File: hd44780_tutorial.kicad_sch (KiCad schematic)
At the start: 28 parts, among them J1 LCD_2004_PinSocket_1x16_P2.54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, J2 USB4105-GF-A, SW1 REG SELECT, SW2 ENABLE, SW3 DS02C-254-1L-08BE

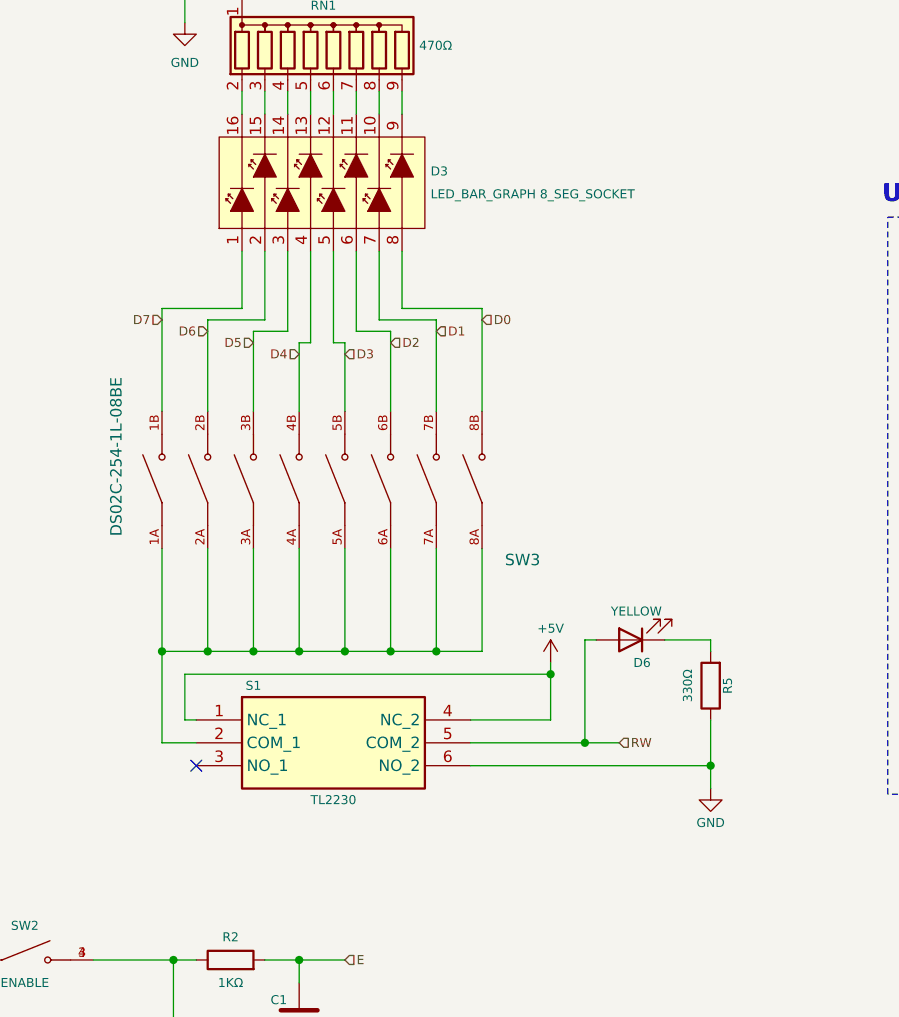
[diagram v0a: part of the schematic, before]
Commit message: Fixed wiring on the TL2230 switch. Made more space between switches and LEDs. New gerbers and JPEG.
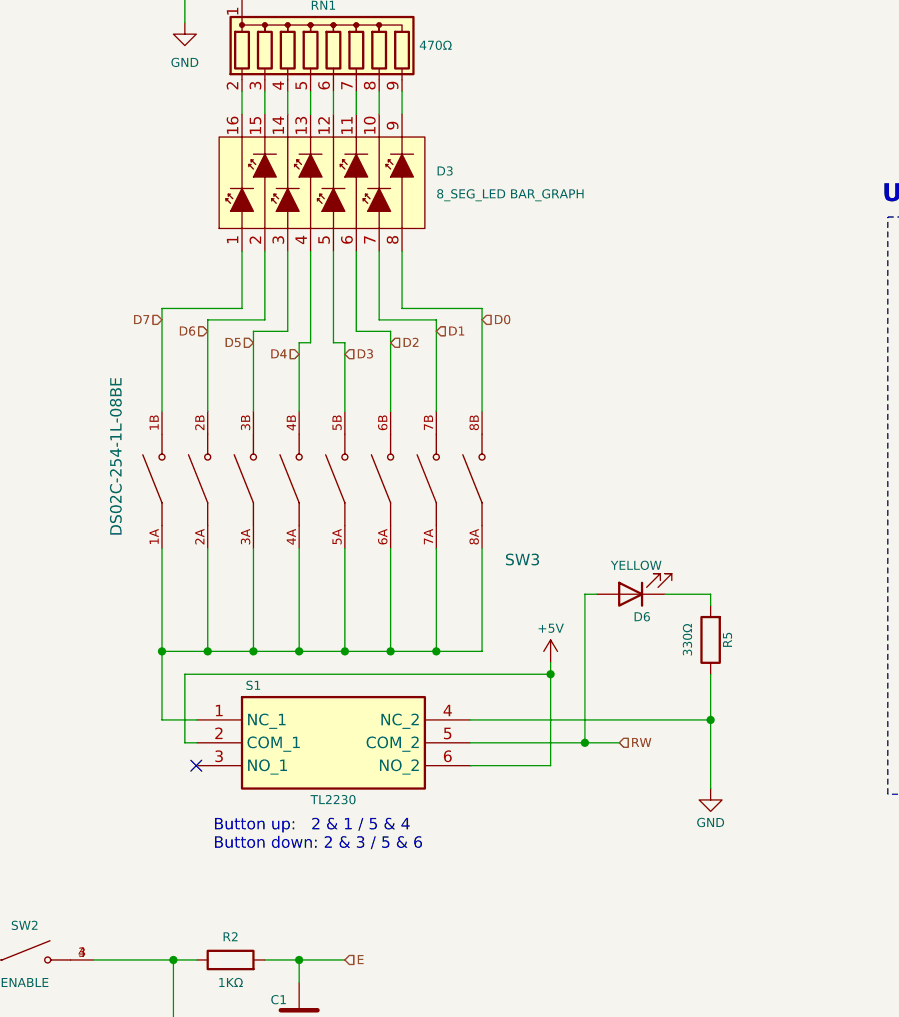
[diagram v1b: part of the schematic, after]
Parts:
- D3: value LED_BAR_GRAPH 8_SEG_SOCKET -> 8_SEG_LED BAR_GRAPH
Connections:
- net +5V: now also S1.2 (COM_1), S1.6 (NO_2); no longer S1.1 (NC_1), S1.4 (NC_2)
- net GND: now also S1.4 (NC_2); no longer S1.6 (NO_2)
- net at SW3.1A, SW3.2A, SW3.3A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: now also S1.1 (NC_1); no longer S1.2 (COM_1)
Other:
- note added: "Button up: 2 & 1 / 5 & 4 Button down: 2 & 3 / 5 & 6"
- moved on the sheet: D6, R5
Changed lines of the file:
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@@
   (title_block
     (title "${project_name}")
-    (date "2024-02-24")
+    (date "2024-03-05")
     (rev "${version}")
   )
@@
   (junction (at 204.47 106.68) (diameter 0) (color 0 0 0 0)
   )
+  (junction (at 58.42 95.25) (diameter 0) (color 0 0 0 0)
+  )
+  (junction (at 133.35 120.65) (diameter 0) (color 0 0 0 0)
+  )
+  (junction (at 58.42 83.82) (diameter 0) (color 0 0 0 0)
+  )
+  (junction (at 102.87 120.65) (diameter 0) (color 0 0 0 0)
+  )
+  (junction (at 17.78 92.71) (diameter 0) (color 0 0 0 0)
+  )
+  (junction (at 163.83 128.27) (diameter 0) (color 0 0 0 0)
+  )
+  (junction (at 118.11 175.26) (diameter 0) (color 0 0 0 0)
+  )
+  (junction (at 128.27 120.65) (diameter 0) (color 0 0 0 0)
+  )
+  (junction (at 204.47 93.98) (diameter 0) (color 0 0 0 0)
+  )
   (junction (at 146.05 123.19) (diameter 0) (color 0 0 0 0)
-  )
-  (junction (at 58.42 95.25) (diameter 0) (color 0 0 0 0)
-  )
-  (junction (at 133.35 120.65) (diameter 0) (color 0 0 0 0)
-  )
-  (junction (at 58.42 83.82) (diameter 0) (color 0 0 0 0)
-  )
-  (junction (at 102.87 120.65) (diameter 0) (color 0 0 0 0)
-  )
-  (junction (at 163.83 133.35) (diameter 0) (color 0 0 0 0)
-  )
-  (junction (at 17.78 92.71) (diameter 0) (color 0 0 0 0)
-  )
-  (junction (at 118.11 175.26) (diameter 0) (color 0 0 0 0)
-  )
-  (junction (at 128.27 120.65) (diameter 0) (color 0 0 0 0)
-  )
-  (junction (at 204.47 93.98) (diameter 0) (color 0 0 0 0)
   )
   (junction (at 149.86 130.81) (diameter 0) (color 0 0 0 0)
@@
     (stroke (width 0) (type default))
   )
-  (wire (pts (xy 151.13 119.38) (xy 149.86 119.38))
+  (wire (pts (xy 151.13 114.3) (xy 149.86 114.3))
     (stroke (width 0) (type default))
   )
@@
     (stroke (width 0) (type default))
   )
-  (wire (pts (xy 105.41 128.27) (xy 105.41 123.19))
-    (stroke (width 0) (type default))
-  )
   (wire (pts (xy 66.04 115.57) (xy 69.85 115.57))
     (stroke (width 0) (type default))
@@
     (stroke (width 0) (type default))
   )
-  (wire (pts (xy 137.16 133.35) (xy 163.83 133.35))
-    (stroke (width 0) (type default))
-  )
   (wire (pts (xy 119.38 86.36) (xy 119.38 76.2))
     (stroke (width 0) (type default))
@@
     (stroke (width 0) (type default))
   )
-  (wire (pts (xy 158.75 119.38) (xy 163.83 119.38))
+  (wire (pts (xy 158.75 114.3) (xy 163.83 114.3))
     (stroke (width 0) (type default))
   )
@@
     (stroke (width 0) (type default))
   )
-  (wire (pts (xy 146.05 123.19) (xy 146.05 128.27))
-    (stroke (width 0) (type default))
-  )
-  (wire (pts (xy 137.16 128.27) (xy 146.05 128.27))
+  (wire (pts (xy 137.16 128.27) (xy 163.83 128.27))
     (stroke (width 0) (type default))
   )
@@
     (stroke (width 0) (type default))
   )
+  (wire (pts (xy 105.41 123.19) (xy 105.41 130.81))
+    (stroke (width 0) (type default))
+  )
   (wire (pts (xy 113.03 120.65) (xy 118.11 120.65))
     (stroke (width 0) (type default))
@@
     (stroke (width 0) (type default))
   )
-  (wire (pts (xy 102.87 120.65) (xy 102.87 130.81))
+  (wire (pts (xy 102.87 120.65) (xy 102.87 128.27))
     (stroke (width 0) (type default))
   )
@@
     (stroke (width 0) (type default))
   )
-  (wire (pts (xy 163.83 119.38) (xy 163.83 120.65))
+  (wire (pts (xy 163.83 114.3) (xy 163.83 115.57))
     (stroke (width 0) (type default))
   )
@@
     (stroke (width 0) (type default))
   )
-  (wire (pts (xy 149.86 119.38) (xy 149.86 130.81))
+  (wire (pts (xy 149.86 114.3) (xy 149.86 130.81))
     (stroke (width 0) (type default))
   )
@@
     (stroke (width 0) (type default))
   )
-  (wire (pts (xy 163.83 133.35) (xy 163.83 135.89))
+  (wire (pts (xy 163.83 128.27) (xy 163.83 135.89))
+    (stroke (width 0) (type default))
+  )
+  (wire (pts (xy 146.05 133.35) (xy 146.05 123.19))
+    (stroke (width 0) (type default))
+  )
+  (wire (pts (xy 137.16 133.35) (xy 146.05 133.35))
     (stroke (width 0) (type default))
   )
@@
     (stroke (width 0) (type default))
   )
-  (wire (pts (xy 163.83 128.27) (xy 163.83 133.35))
+  (wire (pts (xy 163.83 123.19) (xy 163.83 128.27))
     (stroke (width 0) (type default))
   )
@@
     (stroke (width 0) (type default))
   )
-  (wire (pts (xy 106.68 128.27) (xy 105.41 128.27))
-    (stroke (width 0) (type default))
-  )
   (wire (pts (xy 123.19 86.36) (xy 123.19 93.98))
     (stroke (width 0) (type default))
@@
     (stroke (width 0) (type default))
   )
+  (wire (pts (xy 105.41 130.81) (xy 106.68 130.81))
+    (stroke (width 0) (type default))
+  )
   (wire (pts (xy 127 83.82) (xy 133.35 83.82))
     (stroke (width 0) (type default))
@@
     (stroke (width 0) (type default))
   )
+  (wire (pts (xy 102.87 128.27) (xy 106.68 128.27))
+    (stroke (width 0) (type default))
+  )
   (wire (pts (xy 44.45 71.12) (xy 40.64 71.12))
     (stroke (width 0) (type default))
@@
   )
   (wire (pts (xy 128.27 109.22) (xy 128.27 120.65))
-    (stroke (width 0) (type default))
-  )
-  (wire (pts (xy 102.87 130.81) (xy 106.68 130.81))
     (stroke (width 0) (type default))
   )
@@
     (stroke (width 0) (type dash))
     (fill (type none))
+  )
+  (text "Button up:   2 & 1 / 5 & 4\nButton down: 2 & 3 / 5 & 6"
+    (at 108.585 142.875 0)
+    (effects (font (size 1.27 1.27)) (justify left bottom))
   )
   (text "Mounting Holes" (at 21.463 166.751 0)
@@
     )
   )
-  (symbol (lib_id "Device:LED") (at 154.94 119.38 180) (unit 1)
-    (in_bom yes) (on_board yes) (dnp no)
-    (property "Reference" "D6" (at 156.21 121.92 0)
-      (effects (font (size 1 1)))
-    )
-    (property "Value" "YELLOW" (at 155.575 116.205 0)
-      (effects (font (size 1 1)))
-    )
-    (property "Footprint" "LED_THT:LED_D3.0mm" (at 154.94 119.38 0)
-      (effects (font (size 1 1)) hide)
-    )
-    (property "Datasheet" "~" (at 154.94 119.38 0)
+  (symbol (lib_id "Device:LED") (at 154.94 114.3 180) (unit 1)
+    (in_bom yes) (on_board yes) (dnp no)
+    (property "Reference" "D6" (at 156.21 116.84 0)
+      (effects (font (size 1 1)))
+    )
+    (property "Value" "YELLOW" (at 155.575 111.125 0)
+      (effects (font (size 1 1)))
+    )
+    (property "Footprint" "LED_THT:LED_D3.0mm" (at 154.94 114.3 0)
+      (effects (font (size 1 1)) hide)
+    )
+    (property "Datasheet" "~" (at 154.94 114.3 0)
       (effects (font (size 1 1)) hide)
     )
@@
   (symbol (lib_id "hd44780_tutorial:LED_BAR_GRAPH_8_SEG_SOCKET") (at 111.76 68.58 90) (unit 1)
     (in_bom yes) (on_board yes) (dnp no) (fields_autoplaced)
-    (property "Reference" "D3" (at 132.715 67.31 90)
+    (property "Reference" "D3" (at 133.35 67.3099 90)
       (effects (font (size 1 1)) (justify right))
     )
-    (property "Value" "LED_BAR_GRAPH  8_SEG_SOCKET" (at 132.715 69.85 90)
+    (property "Value" " 8_SEG_LED  BAR_GRAPH" (at 133.35 69.8499 90)
       (effects (font (size 1 1)) (justify right))
     )
@@
     )
   )
-  (symbol (lib_id "Device:R") (at 163.83 124.46 180) (unit 1)
-    (in_bom yes) (on_board yes) (dnp no)
-    (property "Reference" "R5" (at 165.735 124.46 90)
-      (effects (font (size 1 1)))
-    )
-    (property "Value" "330Ω" (at 161.29 124.46 90)
-      (effects (font (size 1 1)))
-    )
-    (property "Footprint" "Resistor_THT:R_Axial_DIN0207_L6.3mm_D2.5mm_P7.62mm_Horizontal" (at 165.608 124.46 90)
-      (effects (font (size 1 1)) hide)
-    )
-    (property "Datasheet" "~" (at 163.83 124.46 0)
-      (effects (font (size 1 1)) hide)
-    )
+  (symbol (lib_id "Device:R") (at 163.83 119.38 180) (unit 1)
+    (in_bom yes) (on_board yes) (dnp no)
+    (property "Reference" "R5" (at 165.735 119.38 90)
+      (effects (font (size 1 1)))
+    )
+    (property "Value" "330Ω" (at 161.29 119.38 90)
+      (effects (font (size 1 1)))
+    )
+    (property "Footprint" "Resistor_THT:R_Axial_DIN0207_L6.3mm_D2.5mm_P7.62mm_Horizontal" (at 165.608 119.38 90)
+      (effects (font (size 1 1)) hide)
+    )
+    (property "Datasheet" "~" (at 163.83 119.38 0)
+      (effects (font (size 1 1)) hide)
+    )
